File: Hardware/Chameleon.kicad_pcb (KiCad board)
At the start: 2 copper layers, 88 x 88 mm, 79 parts, among them J1 USB-MICRO-B, P1 PDI, U1 ATXMEGA16A4U-A, U2 AS1121, U3 TLV71333PDBVR, U4 NCP1402

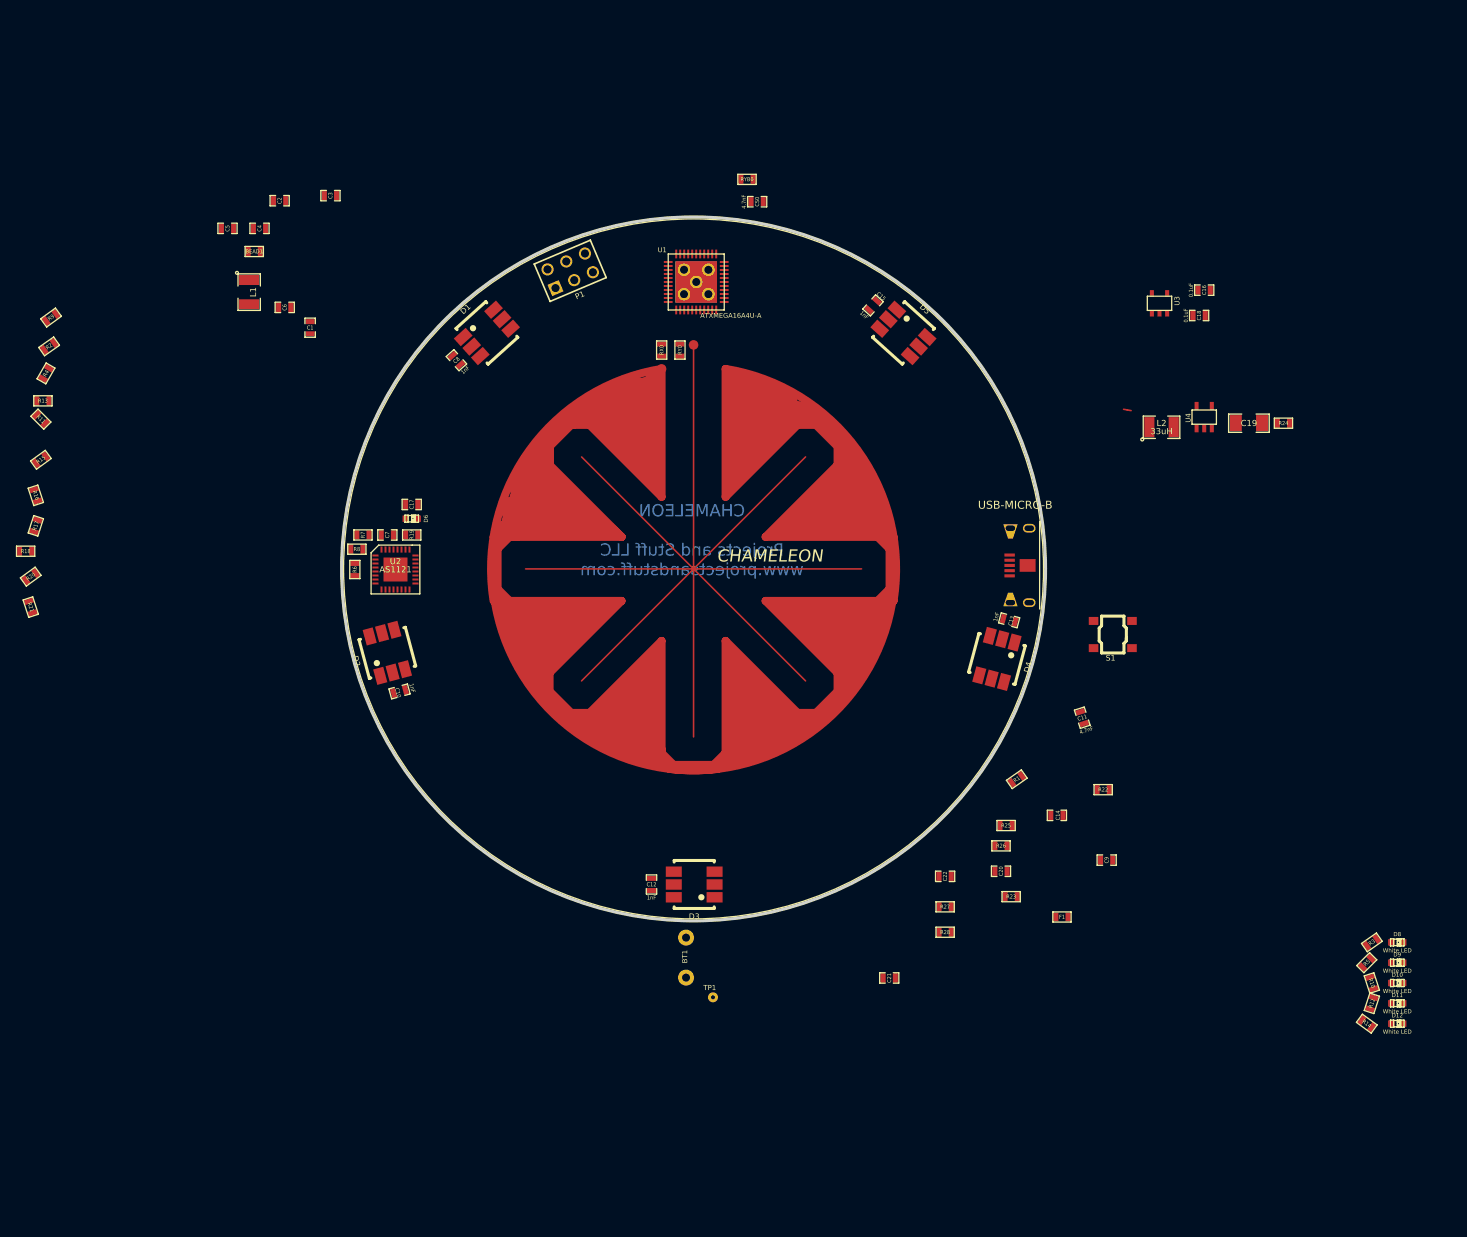
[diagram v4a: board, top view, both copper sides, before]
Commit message: Placed all components, made important routes, and set keepouts for initial autoroute test run.
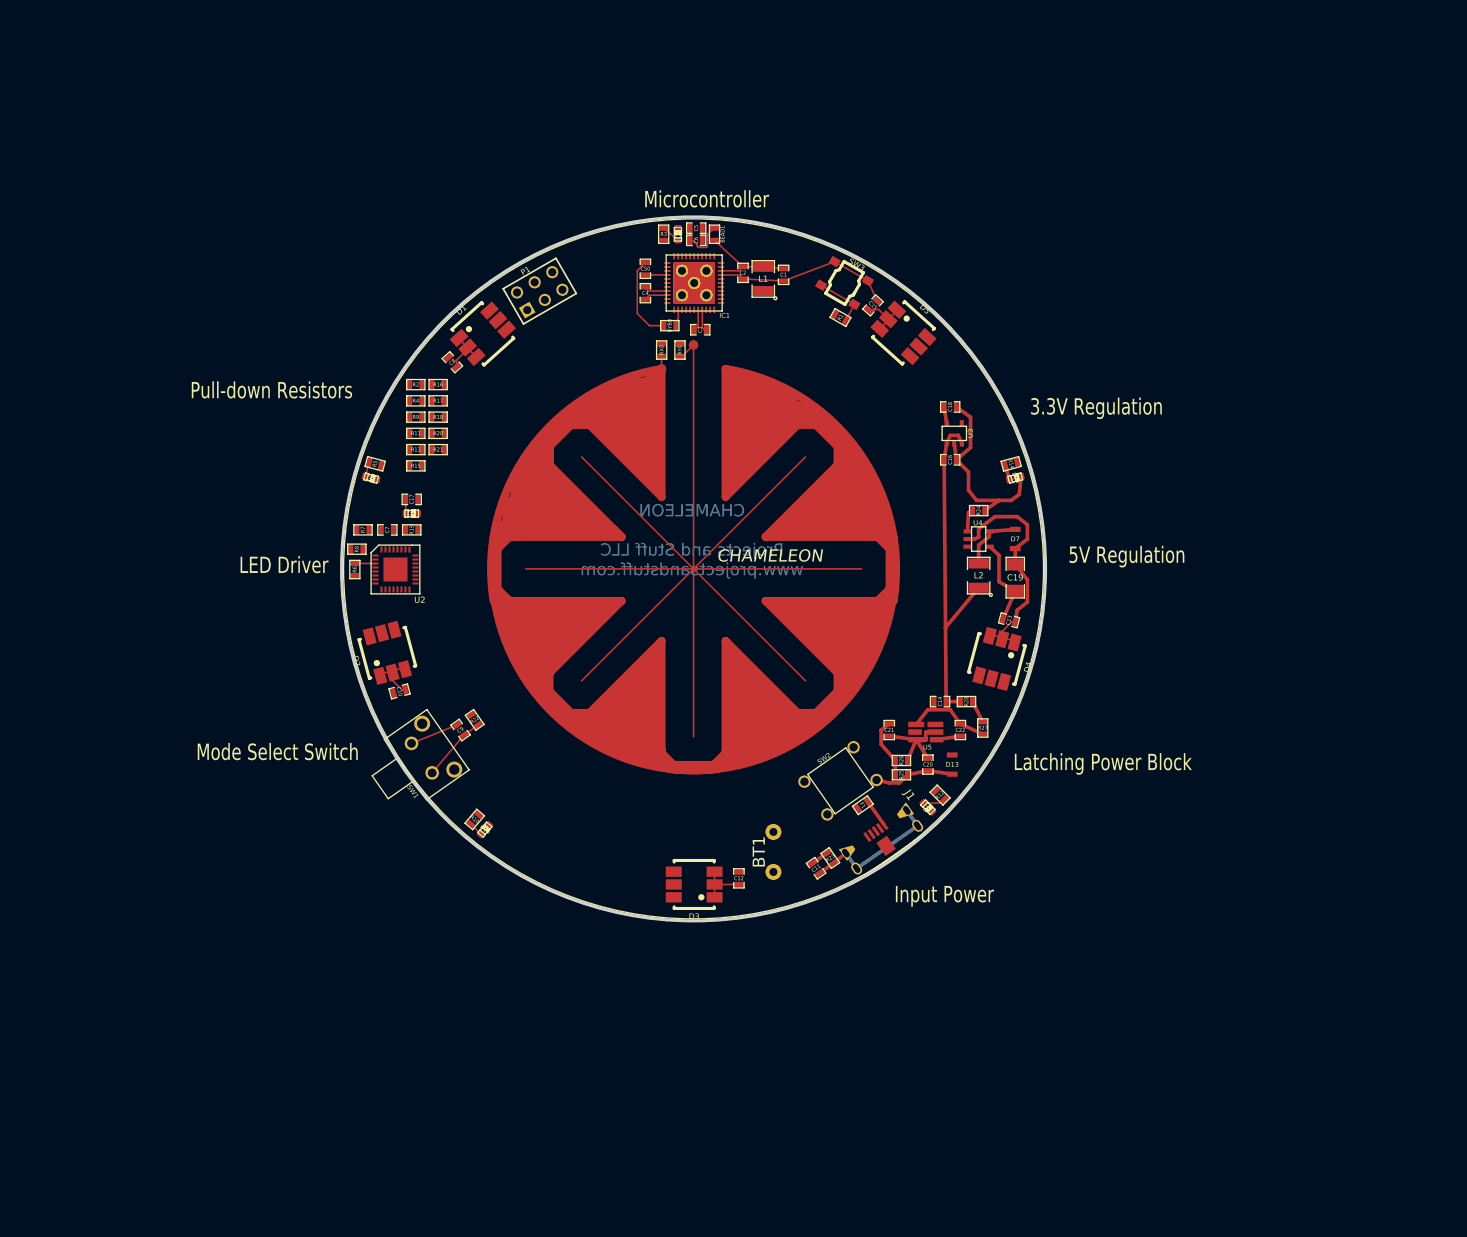
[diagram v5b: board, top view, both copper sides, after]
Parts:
- removed S1: TL3315NF160Q, TL3315NF160Q
- removed TP1: TST, TestPoint_1-pin
- removed U1: ATXMEGA16A4U-A, VQFN44
- added D13: ZLLS410TA, SOD323, F.Cu at (132.3, 124.5)
- added D7: ZLLS410TA, SOD323, F.Cu at (140.2, 96.3)
- added IC1: ATXMEGA16A4U-A-MODIFIED, VQFN44-MODIFIED, F.Cu at (100.1, 64.3)
- added SW1: TL1105JAF160Q, TL1105JAF160Q, F.Cu at (67.1, 122.9)
- added SW2: TL1105SPF250Q, TL1105SPF250Q, F.Cu at (118.4, 126.5)
- added SW3: TL3315NF160Q, TL3315NF160Q, F.Cu at (118.9, 64.3)
- added U5: SI3588DV, TSOP-6-Special, F.Cu at (129.0, 120.4)
- moved D9 141.9 mm to (59.7, 88.6), turned to 345 degrees
- moved R5 138.8 mm to (60.2, 86.9), turned to 165 degrees
- moved D8 126.2 mm to (98.0, 58.2), turned to 90 degrees
- moved R3 125.2 mm to (96.3, 58.2), turned to 90 degrees
- moved D10 115.6 mm to (73.9, 132.6), turned to 50 degrees
- moved R10 114.0 mm to (72.6, 131.3), turned to 230 degrees
- moved D12 83.3 mm to (140.2, 88.6), turned to 15 degrees
- moved R14 82.9 mm to (139.7, 86.9), turned to 195 degrees
- moved C9 82.4 mm to (70.9, 120.1), turned to 125 degrees
- moved R22 79.0 mm to (72.6, 118.9), turned to 305 degrees
- moved L1 64.3 mm to (108.7, 63.8), turned to 90 degrees
- moved D11 63.6 mm to (129.3, 129.8), turned to 315 degrees
- moved R1 61.8 mm to (118.4, 68.6), turned to 330 degrees
- moved R12 59.9 mm to (130.8, 128.3), turned to 315 degrees
- moved C1 59.5 mm to (111.3, 63.2)
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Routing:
- net GND: track 0.00 -> 75.5 mm
- net /VLED: track 0.00 -> 57.4 mm
- net N-0000075: track 0.00 -> 46.8 mm
- net N-000001: track 0.00 -> 18.7 mm
- net /SHIELD: track 0.00 -> 18.1 mm
- net N-0000054: track 0.00 -> 12.4 mm
- net /Y0B: track 0.00 -> 10.7 mm
- net N-0000056: track 0.00 -> 10.4 mm
- net N-0000055: track 0.00 -> 10.0 mm
- net /MODE_SELECT: track 0.00 -> 8.37 mm
- net N-0000057: track 0.00 -> 7.80 mm
- net N-0000053: track 0.00 -> 7.53 mm
- net /PDI_CLK: track 0.00 -> 7.10 mm
- net N-0000058: track 0.00 -> 6.89 mm
- net N-0000060: track 0.00 -> 3.59 mm
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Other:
- board text added: "3.3V Regulation"
- board text added: "5V Regulation"
- board text added: "Input Power"
- board text added: "LED Driver"
- board text added: "Latching Power Block"
- board text added: "Microcontroller"
- board text added: "Mode Select Switch"
- board text added: "Pull-down Resistors"

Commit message: After initial Autoroute attempt, made adjustments to component layout. Iterating again...
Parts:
- moved C17 47.8 mm to (92.2, 130.4), turned to 340 degrees
- moved R6 46.6 mm to (84.2, 138.4), turned to 160 degrees
- moved R7 46.1 mm to (81.8, 135.0), turned to 70 degrees
- moved D6 44.2 mm to (89.5, 129.7), turned to 160 degrees
- moved C7 42.5 mm to (82.9, 132.0), turned to 250 degrees
- moved U2 42.0 mm to (87.4, 134.1), turned to 70 degrees
- moved R8 42.0 mm to (79.8, 133.3), turned to 70 degrees
- moved R19 38.9 mm to (84.1, 128.9), turned to 70 degrees
- moved R21 20.7 mm to (60.3, 104.3)
- moved R18 20.5 mm to (60.8, 100.2)
- moved R20 20.5 mm to (60.8, 102.2)
- moved R17 20.3 mm to (61.3, 98.2)
- moved R16 20.3 mm to (61.3, 96.1)
- moved R13 8.02 mm to (61.3, 92.1)
- moved R15 8.02 mm to (61.3, 94.1)
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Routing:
- net /Y0A: track 2.75 -> 23.5 mm
- net N-0000058: track 6.89 -> 0.00 mm
- net /X0: track 0.00 -> 4.92 mm
- net N-000001: track 18.7 -> 13.9 mm
- net /AS_MODE: track 2.58 -> 0.00 mm
- net N-0000075: track 46.8 -> 44.3 mm
- net N-0000068: track 2.33 -> 0.00 mm
- net /VLED: track 57.4 -> 55.6 mm
- net GND: track 75.5 -> 74.0 mm
